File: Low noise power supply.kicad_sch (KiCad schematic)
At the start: 160 parts, among them K1 RZ03-1A4-D012, Q1 BC817, Q2 BC807, Q3 BC817, U1 LM317T, U2 LT3045xMSE, U3 LT3045xMSE, U4 LM317T, U5 LT3045xMSE, U6 LT3045xMSE, U7 LM317T, U8 LT3045xMSE, U9 LT3045xMSE

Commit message: one resistor mpn change
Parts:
- R10, R22, R25, R31, R34, R7: MPN AC0805FR-071KL -> RC0805FR-071KL
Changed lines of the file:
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@@
 			)
 		)
-		(property "MPN" "AC0805FR-071KL"
+		(property "MPN" "RC0805FR-071KL"
 			(at 354.33 88.9 90)
 			(effects
@@
 			)
 		)
-		(property "MPN" "AC0805FR-071KL"
+		(property "MPN" "RC0805FR-071KL"
 			(at 203.2 157.48 90)
 			(effects
@@
 			)
 		)
-		(property "MPN" "AC0805FR-071KL"
+		(property "MPN" "RC0805FR-071KL"
 			(at 203.2 101.6 90)
 			(effects
@@
 			)
 		)
-		(property "MPN" "AC0805FR-071KL"
+		(property "MPN" "RC0805FR-071KL"
 			(at 354.33 200.66 90)
 			(effects
@@
 			)
 		)
-		(property "MPN" "AC0805FR-071KL"
+		(property "MPN" "RC0805FR-071KL"
 			(at 203.2 213.36 90)
 			(effects
@@
 			)
 		)
-		(property "MPN" "AC0805FR-071KL"
+		(property "MPN" "RC0805FR-071KL"
 			(at 354.33 144.78 90)
 			(effects

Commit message: changing power-on system
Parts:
- removed D3: BZV55C12, symbol Diode:BZV55C12
- removed Q1, Q3: BC817, Package_TO_SOT_SMD:SOT-23, symbol Transistor_BJT:BC817
- removed Q2: BC807, Package_TO_SOT_SMD:SOT-23, symbol Transistor_BJT:BC807
- removed R13, R15: 47k, symbol Device:R
- removed R14: 2k2, symbol Device:R
- removed R16: 750, symbol Device:R
- removed R19: 69.8, symbol Device:R
- removed R28: 64.9, symbol Device:R
- removed R4: 22, symbol Device:R
- added C5: 10u, symbol Device:C_Polarized
- added C6: 10u, symbol Device:C
- added C7: 1u, symbol Device:C
- added D1: 1N4007L, symbol Diode:1N4001
- added U1: NE555D, Package_SO:SOIC-8_3.9x4.9mm_P1.27mm, symbol Timer:NE555D
- R13: renamed from R18; value 825 -> 909; MPN RC0805FR-07825RL -> RC0805FR-07909RL
- R2: renamed from R11; value 240 -> 4k7; MPN RC0805FR-07240RL -> RC0805FR-074K7L
- R21: renamed from R27; value 511 -> 576; MPN RC0805FR-07511RL -> RC0805FR-07576RL
- R3: renamed from R12; value 240 -> 91k; MPN RC0805FR-07240RL -> RC0805FR-0791KL
- R5: renamed from R3; value 2k2 -> 2k26; MPN RC0805FR-072K2L -> RC0805FR-072K26L
- renumbered C7 to C10, C8 to C11, C9 to C12, C10 to C13, C11 to C14, C12 to C15, C13 to C16, C14 to C17, C15 to C18, C16 to C19, C17 to C20, C18 to C21, C19 to C22, C20 to C23, C21 to C24, C22 to C25, C23 to C26, C24 to C27, C25 to C28, C26 to C29, C4 to C3, C27 to C30, C28 to C31, C29 to C32, C30 to C33, C31 to C34, C32 to C35, C33 to C36, C34 to C37, C35 to C38, C37 to C39, C3 to C4, C38 to C40, C39 to C41, C40 to C42, C41 to C43, C36 to C44, C43 to C45, C44 to C46, C45 to C47, C46 to C48, C47 to C49, C48 to C50, C84 to C51, C85 to C52, C42 to C53, C49 to C54, C50 to C55, C52 to C56, C53 to C57, C54 to C58, C55 to C59, C56 to C60, C51 to C61, C58 to C62, C59 to C63, C60 to C64, C61 to C65, C62 to C66, C63 to C67, C65 to C68, C66 to C69, C57 to C70, C64 to C71, C67 to C72, C69 to C73, C70 to C74, C71 to C75, C72 to C76, C73 to C77, C68 to C78, C75 to C79, C5 to C8, C76 to C80, C77 to C81, C78 to C82, C79 to C83, C80 to C84, C82 to C85, C83 to C86, C74 to C87, C81 to C88, C6 to C9, D1 to D3, R5 to R10, R6 to R11, R17 to R12, R25 to R14, R22 to R15, R23 to R16, R24 to R17, R20 to R18, R21 to R19, R26 to R20, R34 to R22, R31 to R23, R32 to R24, R33 to R25, R29 to R26, R30 to R27, R2 to R4, R10 to R6, U9 to U10, U1 to U2, U2 to U3, U3 to U4, U4 to U5, U5 to U6, U6 to U7, U7 to U8, U8 to U9
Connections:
- net ENABLE: now also D3.1 (K), K1.A1, U1.3 (OUT)
- net GND: now also D2.2 (A), D3.2 (A), K1.A2, R13.2, R21.2, R5.2, C6.2, C7.2, U1.1 (GND)
- net at K1.14, PS1.3 (+Vout), R1.1: now also D1.2 (A); no longer D2.2 (A)
- net at R2.1: now also C5.1, C6.1, D1.1 (K), U1.8 (VCC)
- net at R3.1: now also D2.1 (K), C5.2, U1.2 (TRIG), U1.6 (THRES); no longer R2.2
- new net: C7.1, R2.2, U1.4 (~{RST})
- no-connect marks 6 -> 8
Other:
- note removed: "R3, R4, R5, R6, 18, R19, R20, R21, R27, R28, R29, R30 ряд Е96 точность 1%"
- moved on the sheet: C3, C4, D3, K1, R1, R2, R3

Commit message: add PWM second stage tabiliser
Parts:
- removed C42, C52, C72, C73, C76, C86: 100u, symbol Device:C_Polarized
- removed C43, C45, C50, C51, C61, C77, C78, C79, C84, C85: 10u, symbol Device:C
- removed C46, C47, C48, C49, C80, C81, C82, C83: 220u, symbol Device:C_Polarized
- removed C53, C87, C88: 1u, symbol Device:C
- removed C74, C75: 1000u, symbol Device:C_Polarized
- removed CT11, CT12, CT13, CT14, CT15, CT2, CT3, CT4, CT5: 33u, symbol Device:C_Polarized
- removed D5, D6: 1N4007L, symbol Diode:1N4001
- removed R11: 56k2, symbol Device:R
- removed R15, R22, R23, R6: 1k, symbol Device:R
- removed R20: 240, symbol Device:R
- removed R21: 576, symbol Device:R
- removed R24, R25, R8, R9: 0.2, symbol Device:R
- removed R26: 100, symbol Device:R
- removed R27: 16k5, symbol Device:R
- removed U10, U3, U4, U9: LT3045xMSE, Package_SO:MSOP-12-1EP_3x4.039mm_P0.65mm_EP1.651x2.845mm, symbol Regulator_Linear:LT3045xMSE
- removed U5, U8: LM317T, Package_TO_SOT_THT:TO-220-3_Vertical, symbol Regulator_Linear:LM317_TO-220
- added C57, C58: 10u, symbol Device:C
- added C62: 150p, symbol Device:C
- added D5: BAT54J, Diode_SMD:D_SOD-323F, symbol Diode:BAT54J
- added D6: B340, Diode_SMD:D_SMC, symbol Diode:B340
- added R12: 20k, symbol Device:R
- added R13: 10k, symbol Device:R
- added R16: 147k, symbol Device:R
- added U5: L78L05, Package_TO_SOT_SMD:SOT-23_Handsoldering, symbol Regulator_Linear:L78L05_SOT89
- added U6: MP1584EN, Package_SO:SOIC-8-1EP_3.9x4.9mm_P1.27mm_EP2.62x3.51mm, symbol Regulator_Switching:MP2303ADN
- C54: value 1u -> 100n; MPN C2012B105K500NT2 -> C3225B106K500NT
- L4: value 220u -> 22u; MPN CDRH127/LDNP-221MC -> SLF12565T-220M3R5-PF
- R10: value 4k3 -> 10k; MPN RC0805FR-074K3L -> RC0805FR-074K99L
- R11: renamed from R18; value 4k99 -> 4k3
- R14: value 1k -> 180k; MPN RC0805FR-071KL -> RC0805FR-07240RL
- R15: renamed from R12; value 240 -> 300k
- R17: renamed from R13; value 909 -> 19k6
- R7: value 1k -> 20k; MPN RC0805FR-071KL -> RC0805FR-07240RL
- R9: renamed from R19; value 20k -> 56k2
- renumbered C15 to C10, C16 to C11, C17 to C12, C5 to C13, C18 to C14, C19 to C15, C20 to C16, C21 to C17, C22 to C18, C23 to C19, C24 to C20, C25 to C21, C26 to C22, C27 to C23, C3 to C24, C4 to C25, C28 to C26, C29 to C27, C30 to C28, C31 to C29, C8 to C3, C32 to C30, C33 to C31, C34 to C32, C35 to C33, C36 to C34, C37 to C35, C6 to C36, C7 to C37, C9 to C4, C69 to C42, C68 to C43, C67 to C44, C66 to C45, C65 to C46, C71 to C47, C44 to C48, C59 to C49, C10 to C5, C60 to C50, C62 to C51, C63 to C52, C64 to C53, C70 to C55, C55 to C56, C56 to C59, C11 to C6, C57 to C60, C58 to C61, C12 to C7, C13 to C8, C14 to C9, CT10 to CT2, CT9 to CT3, CT7 to CT4, CT8 to CT5, R17 to R4, R4 to R5, R5 to R6, R16 to R8, U7 to U3, U6 to U4
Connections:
- net +5V is gone; now on net +12V: C46.1, C53.1, R4.1, R8.2
- net +13V: now also C42.1, C43.1, C49.1, C50.1, C59.1, C60.1, C61.1, CT2.1, CT4.1, CT6.1, L4.2, R15.2, U3.1 (IN), U3.2 (IN), U3.3 (IN), U3.7 (PGFB), U4.1 (IN), U4.2 (IN), U4.3 (IN), U4.7 (PGFB), C58.2
- net +15V: no longer L4.1
- net ENABLE: now also R12.1; no longer R14.1
- net GND: now also R10.2, R11.2, R14.2, C57.1, C58.1, D6.2 (A), R13.2, R16.2, U5.2 (GND), U6.5 (GND); no longer C54.2, R10.1, R11.1
- net at C54.1: now also D5.1 (K), U6.8 (BST)
- net at U3.4 (EN/UV): now also R10.1, R7.2, U4.4 (EN/UV); no longer R14.2
- net at C56.1, L3.2: now also C57.2, U5.3 (IN), U6.7 (VIN)
- net at R17.1: now also R15.1, U6.4 (FB); no longer R15.2
- net at R9.2: now also R11.1; no longer R11.2
- removed net +6V: C42.1, C43.1, C49.1, C50.1, C59.1, C60.1, C61.1, CT2.1, CT4.1, CT6.1, R15.1, U3.1 (IN), U3.2 (IN), U3.3 (IN), U3.7 (PGFB), U4.1 (IN), U4.2 (IN), U4.3 (IN), U4.7 (PGFB)
- new net: R12.2, R13.1, U6.2 (EN)
- new net: D5.2 (A), U5.1 (OUT)
- new net: C62.1, U6.3 (COMP)
- new net: C62.2, R16.1
- new net: C54.2, D6.1 (K), L4.1, U6.1 (SW)
- new net: R14.1, U6.6 (FREQ)
- no-connect marks 8 -> 4
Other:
- note added: "R4 и R8 выполнить медными проводниками на плате в виде дорожек определенной длины и ширины:"
- note added: "Вариант 1 - линейный понижающий мтабилизатор"
- note added: "Вариант 2 - ШИМ понижающий мтабилизатор"
- note added: "Основная плата"
- note added: "Плата оконечного каскада стабилизации"
- note removed: "R8, R9, R23, R24, R32, R33 выполнить медными проводниками на плате в виде дорожек определенной длины и ширины:"
- moved on the sheet: C1, C10, C11, C12, C13, C14, C15, C16, C17, C18, C19, C2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

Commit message: bom fix
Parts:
- C55: renamed from C54; MPN C3225B106K500NT -> 08055C104K4T2A
- C62: MPN C3225B106K500NT -> CC0805JRNPO0BN151
- C7: renamed from C37; MPN 08053C105KAT2A -> C2012B105K500NT2
- D5: MPN (none) -> BAT54J
- R12: MPN RC0805FR-07240RL -> RC0805FR-0720KL
- R13: MPN RC0805FR-07240RL -> RC0805FR-0710KL
- R14: MPN RC0805FR-07240RL -> RC0805FR-07180KL
- R15: MPN RC0805FR-07240RL -> RC0805FR-07300KL
- R16: MPN RC0805FR-07240RL -> RC0805FR-07147KL
- R17: MPN RC0805FR-07909RL -> RC0805FR-0719K6L
- R5: renamed from R7; MPN RC0805FR-07240RL -> RC0805FR-0720KL
- R7: renamed from R9; MPN RC0805FR-0720KL -> RC0805FR-0756K2L
- R8: renamed from R10; MPN RC0805FR-074K99L -> RC0805FR-0710KL
- R9: renamed from R11; MPN RC0805FR-074K99L -> RC0805FR-074K3L
- renumbered C5 to C10, C6 to C11, C7 to C12, C8 to C13, C9 to C14, C10 to C15, C11 to C16, C12 to C17, C14 to C18, C15 to C19, C16 to C20, C17 to C21, C18 to C22, C19 to C23, C20 to C24, C21 to C25, C22 to C26, C23 to C27, C26 to C28, C27 to C29, C24 to C3, C28 to C30, C29 to C31, C30 to C32, C31 to C33, C32 to C34, C33 to C35, C34 to C36, C35 to C37, C42 to C38, C43 to C39, C25 to C4, C44 to C40, C45 to C41, C46 to C42, C47 to C43, C49 to C44, C50 to C45, C51 to C46, C52 to C47, C53 to C48, C55 to C49, C13 to C5, C38 to C50, C39 to C51, C40 to C52, C41 to C53, C48 to C54, C36 to C6, C3 to C8, C4 to C9, CT2 to CT1, CT3 to CT2, CT4 to CT3, CT5 to CT4, CT1 to CT5, R5 to R10, R6 to R11, R8 to R6, U3 to U2, U4 to U3, U2 to U4

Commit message: reverse power-on system manage BOM excel file
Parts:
- removed C5: 10u, symbol Device:C_Polarized
- removed C6: 10u, symbol Device:C
- removed C7: 1u, symbol Device:C
- removed D2: 1N4007L, symbol Diode:1N4001
- removed U1: NE555D, Package_SO:SOIC-8_3.9x4.9mm_P1.27mm, symbol Timer:NE555D
- added D3: BZV55C12, symbol Diode:BZV55C12
- added Q1, Q3: BC817, Package_TO_SOT_SMD:SOT-23, symbol Transistor_BJT:BC817
- added Q2: BC807, Package_TO_SOT_SMD:SOT-23, symbol Transistor_BJT:BC807
- added R4: 47k, symbol Device:R
- added R5: 2k2, symbol Device:R
- added R6, R7: 240, symbol Device:R
- R2: value 4k7 -> 750; MPN RC0805FR-074K7L -> RC0805FR-07750RL
- R3: value 91k -> 47k; MPN RC0805FR-0791KL -> RC0805FR-0747KL
- renumbered C13 to C10, C14 to C11, C15 to C12, C16 to C13, C17 to C14, C18 to C15, C19 to C16, C20 to C17, C21 to C18, C22 to C19, C23 to C20, C24 to C21, C25 to C22, C26 to C23, C27 to C24, C28 to C25, C29 to C26, C30 to C27, C31 to C28, C32 to C29, C33 to C30, C34 to C31, C35 to C32, C36 to C33, C37 to C34, C38 to C35, C39 to C36, C40 to C37, C41 to C38, C42 to C39, C43 to C40, C44 to C41, C45 to C42, C46 to C43, C47 to C44, C48 to C45, C49 to C46, C50 to C47, C51 to C48, C52 to C49, C8 to C5, C53 to C50, C54 to C51, C55 to C52, C56 to C53, C57 to C54, C58 to C55, C59 to C56, C60 to C57, C61 to C58, C62 to C59, C9 to C6, C10 to C7, C11 to C8, C12 to C9, D3 to D2, R6 to R10, R7 to R11, R8 to R12, R9 to R13, R10 to R14, R11 to R15, R12 to R16, R13 to R17, R14 to R18, R15 to R19, R16 to R20, R17 to R21, R4 to R8, R5 to R9, U2 to U1, U3 to U2, U4 to U3, U5 to U4, U6 to U5
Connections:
- net +15V: now also D3.1 (K), Q2.2 (E), R4.2
- net ENABLE: now also R2.1, R3.2, Q2.3 (C); no longer D2.1 (K), K1.A1
- net GND: now also R3.1, Q1.2 (E), Q3.2 (E), R7.2; no longer D2.2 (A), K1.A2, R3.2
- net at D1.1 (K): now also D2.1 (K), K1.A1; no longer R2.1
- net at R2.2: now also Q1.1 (B)
- new net: D2.2 (A), K1.A2, Q1.3 (C)
- new net: D3.2 (A), R6.1
- new net: Q3.1 (B), R6.2, R7.1
- new net: Q3.3 (C), R5.1
- new net: Q2.1 (B), R4.1, R5.2
- no-connect marks 4 -> 2
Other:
- note added: "R8 и R10 выполнить медными проводниками на плате в виде дорожек определенной длины и ширины:"
- note removed: "R4 и R8 выполнить медными проводниками на плате в виде дорожек определенной длины и ширины:"
- moved on the sheet: D2, K1, R1

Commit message: syntax fix
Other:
- note added: "Вариант 1 - линейный понижающий cтабилизатор"
- note added: "Вариант 2 - ШИМ понижающий cтабилизатор"
- note removed: "Вариант 1 - линейный понижающий мтабилизатор"
- note removed: "Вариант 2 - ШИМ понижающий мтабилизатор"
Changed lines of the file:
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@@
 		)
 	)
-	(text "Вариант 2 - ШИМ понижающий мтабилизатор"
+	(text "Вариант 2 - ШИМ понижающий cтабилизатор"
 		(exclude_from_sim no)
 		(at 48.26 211.836 0)
@@
 		)
 	)
-	(text "Вариант 1 - линейный понижающий мтабилизатор"
+	(text "Вариант 1 - линейный понижающий cтабилизатор"
 		(exclude_from_sim no)
 		(at 49.784 137.414 0)

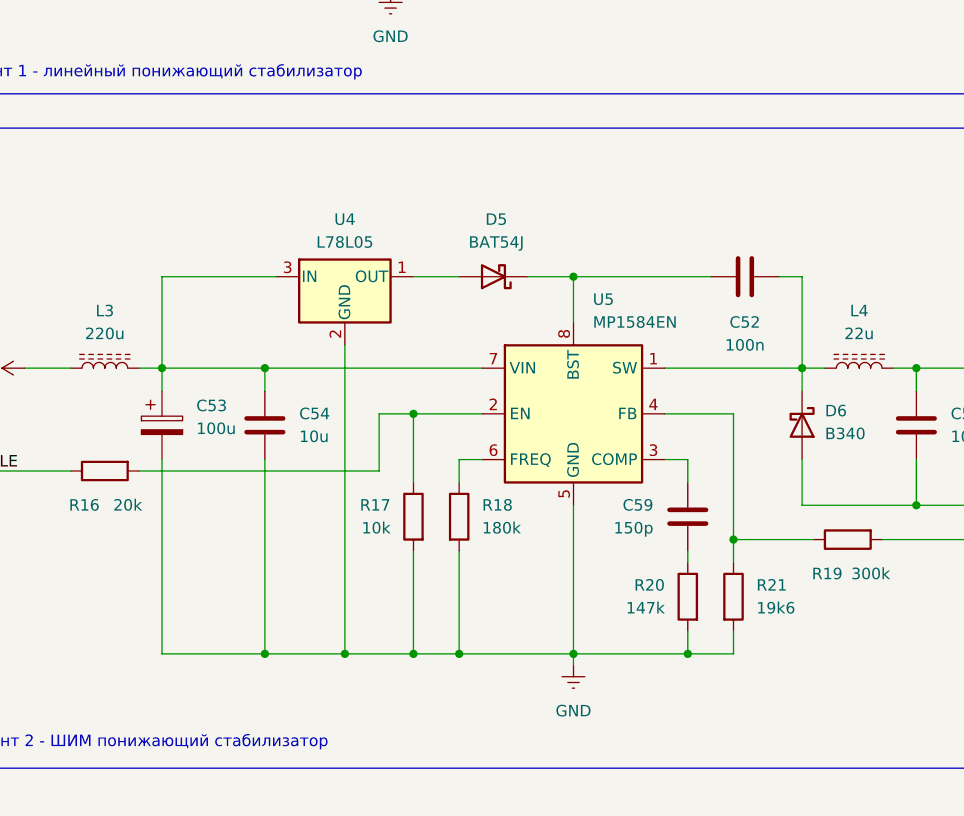
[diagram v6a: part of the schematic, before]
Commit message: add shunt capactors to 78L05
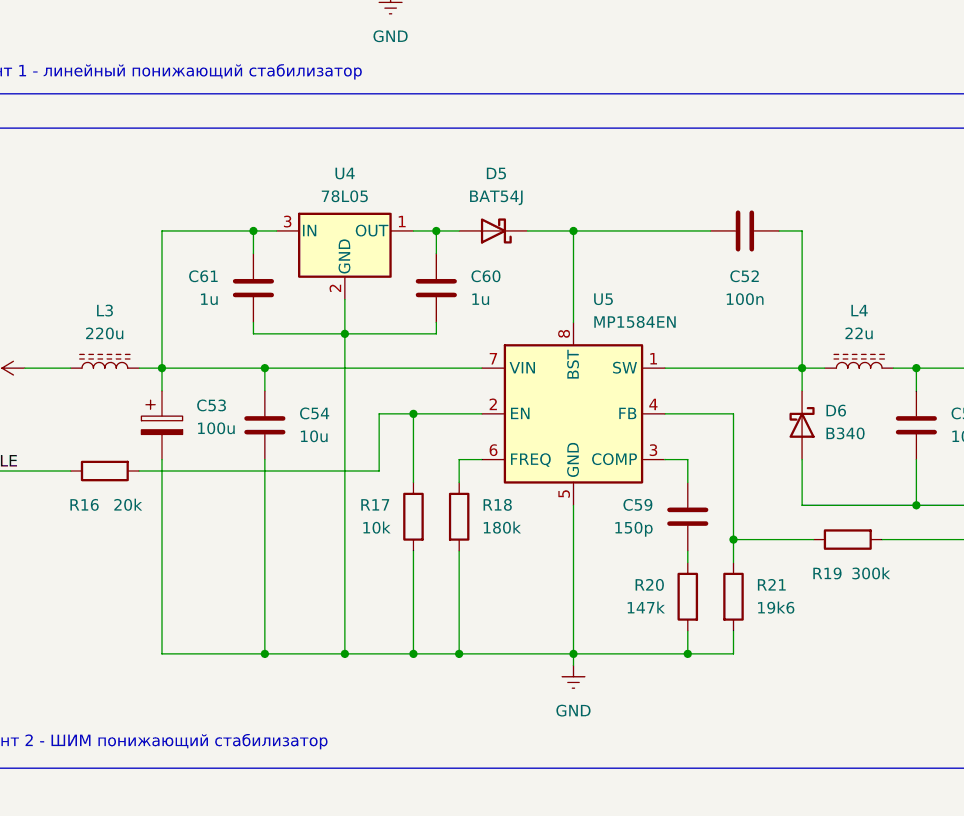
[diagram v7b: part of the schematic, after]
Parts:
- added C60, C61: 1u, symbol Device:C
- U4: value L78L05 -> 78L05; MPN L78L05 -> 78L05
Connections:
- net GND: now also C60.2, C61.2
- net at D5.2 (A), U4.1 (OUT): now also C60.1
- net at C53.1, C54.2, L3.2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: now also C61.1
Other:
- moved on the sheet: C52, D5, U4

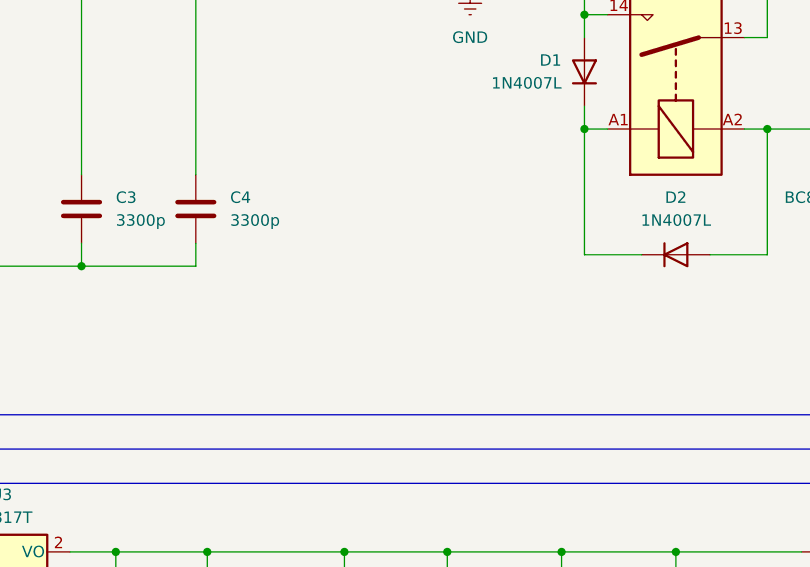
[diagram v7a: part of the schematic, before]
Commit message: add primary secondary connection
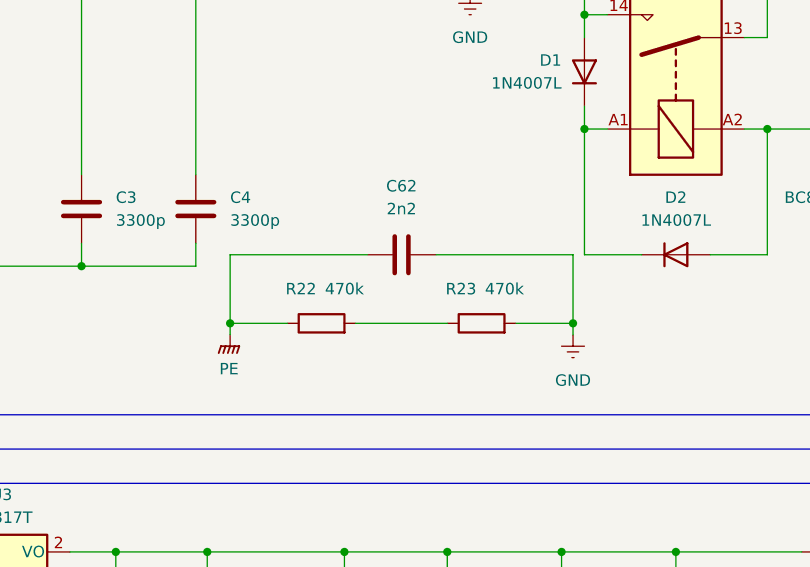
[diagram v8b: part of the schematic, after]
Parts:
- added C62: 2n2, symbol Device:C
- added R22, R23: 470k, symbol Device:R
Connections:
- net GND: now also C62.2, R23.2
- net PE: now also C62.1, R22.1
- new net: R22.2, R23.1
